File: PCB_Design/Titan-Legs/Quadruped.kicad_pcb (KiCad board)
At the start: 4 copper layers, 55.6 x 55.5 mm, 102 parts, among them IC1 TPS54260DGQR, IC2 CP2102, IC3 DRV8323RSRGZT, J1 TYPE-C-31-M-12, J2 691214110003, P1 282837-2, P2 282837-2, Q1 BSC031N06NS3GATMA1, Q2 BSC031N06NS3GATMA1, Q3 BSC031N06NS3GATMA1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

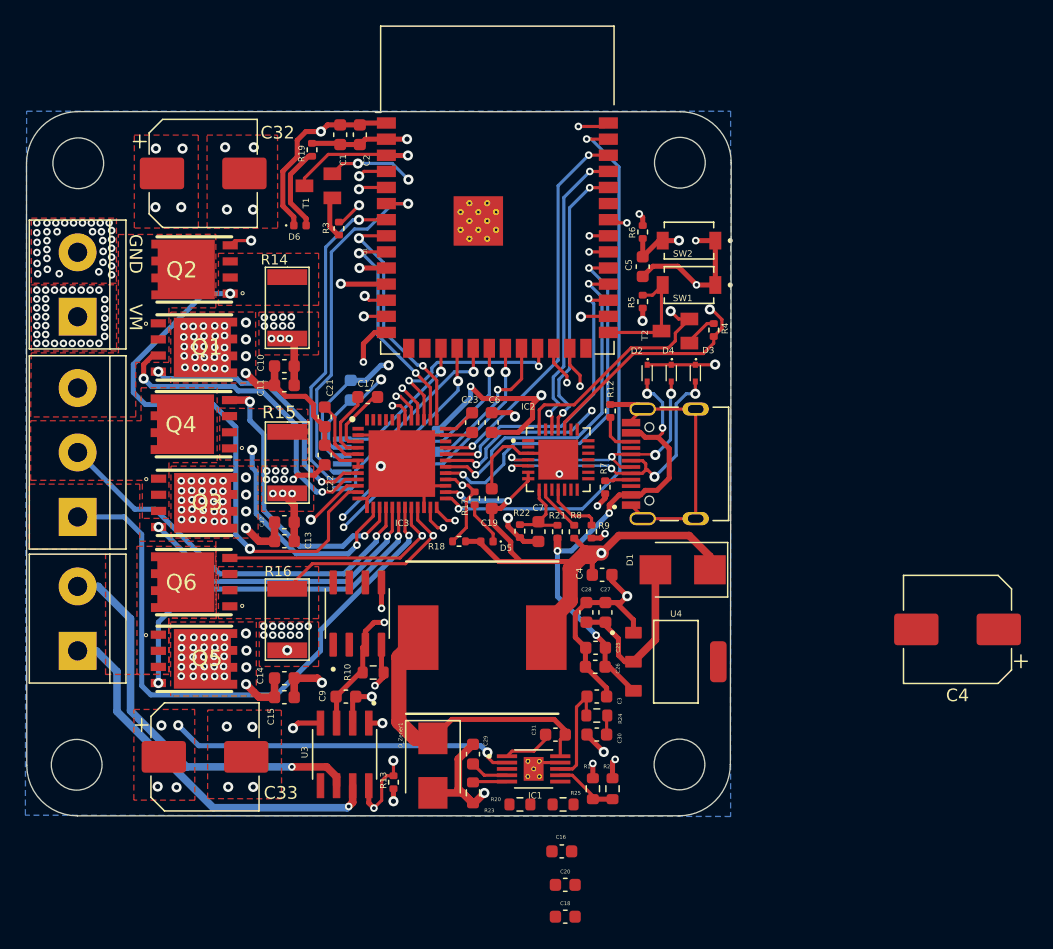
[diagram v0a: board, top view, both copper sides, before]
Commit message: Added Electrolytic Capacitor and moved AMS1117 to B.Cu
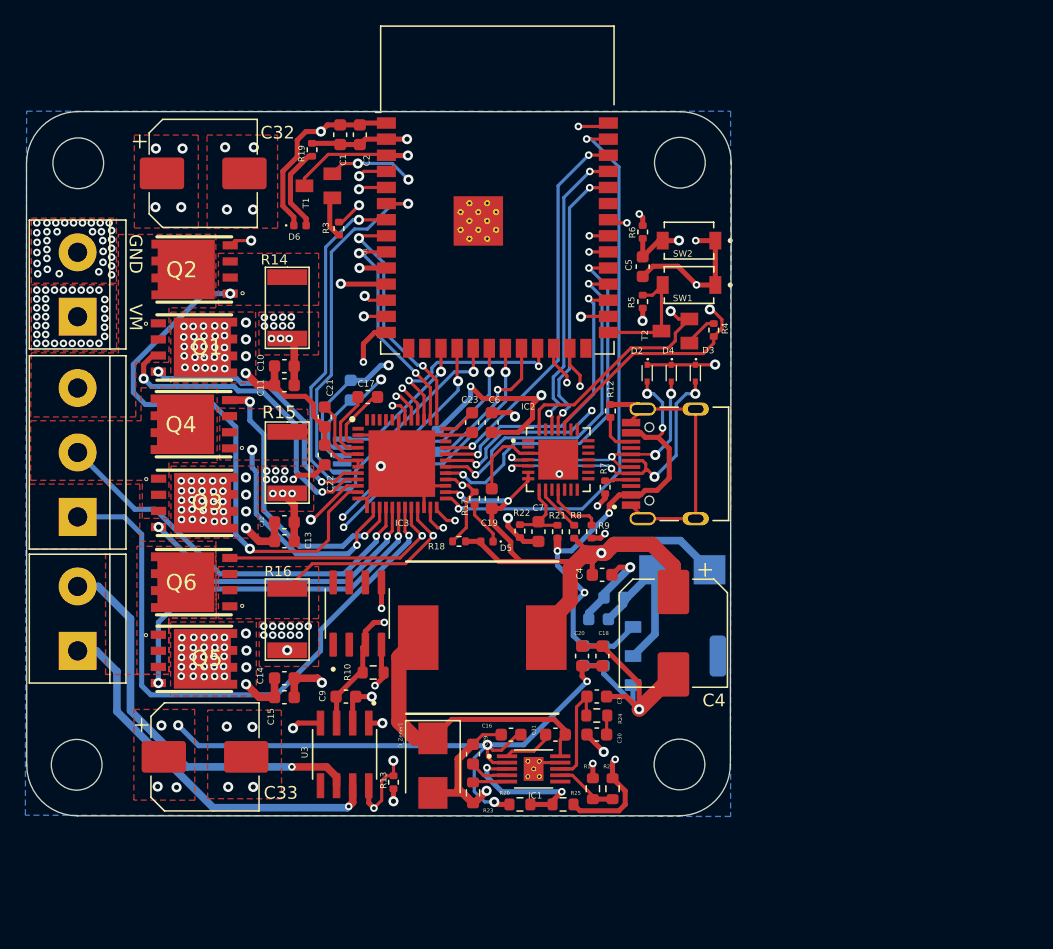
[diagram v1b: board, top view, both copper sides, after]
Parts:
- C25, C26, C27, C28, D1, U4: moved to B.Cu
- moved C4 22.4 mm to (79.8, 116.5), turned to -90 degrees
- moved C18 20.8 mm to (74.2, 118.2), turned to -90 degrees
- moved C20 18.1 mm to (72.6, 118.2), turned to -90 degrees
- moved C16 10.0 mm to (67.0, 124.5)
- moved C28 2.45 mm to (75.1, 113.7), turned to 180 degrees
- moved C26 1.28 mm to (72.7, 118.2), turned to -90 degrees
- moved C25 0.91 mm to (74.3, 118.2), turned to -90 degrees
- moved C27 0.76 mm to (73.9, 115.3), turned to 180 degrees
- moved U4 0.45 mm to (79.9, 118.2)
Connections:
- IC1 pad 13: (no net) -> GND
- IC1 pad 14: (no net) -> GND
- IC1 pad 3: /EN -> /EN-TPS
- R20 pad 2: /EN -> /EN-TPS
- R25 pad 1: /EN -> /EN-TPS
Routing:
- net VM: track 50.8 -> 74.7 mm, vias 127 -> 129
- net GND: track 166.4 -> 188.0 mm, vias 94 -> 95
- net /EN-TPS: track 0.00 -> 11.8 mm, vias 0 -> 2
- net 3V3_IN: track 100.7 -> 108.5 mm
- net /ESP_3V3: track 13.9 -> 13.1 mm
